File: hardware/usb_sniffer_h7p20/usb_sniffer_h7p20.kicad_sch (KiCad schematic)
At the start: 98 parts, among them J4 USB_C_Receptacle_USB2.0_16P, J5 FFC-40P-0.5mm,NC, U1 H7P20N0L128-M3H1, U6 P25Q32SH-SSH-IT, U7 CY7C68013A-56LTX, U8 24C64BN, U9 CJ3439KDW, X1 XO32,26M,NC, Y2 24M

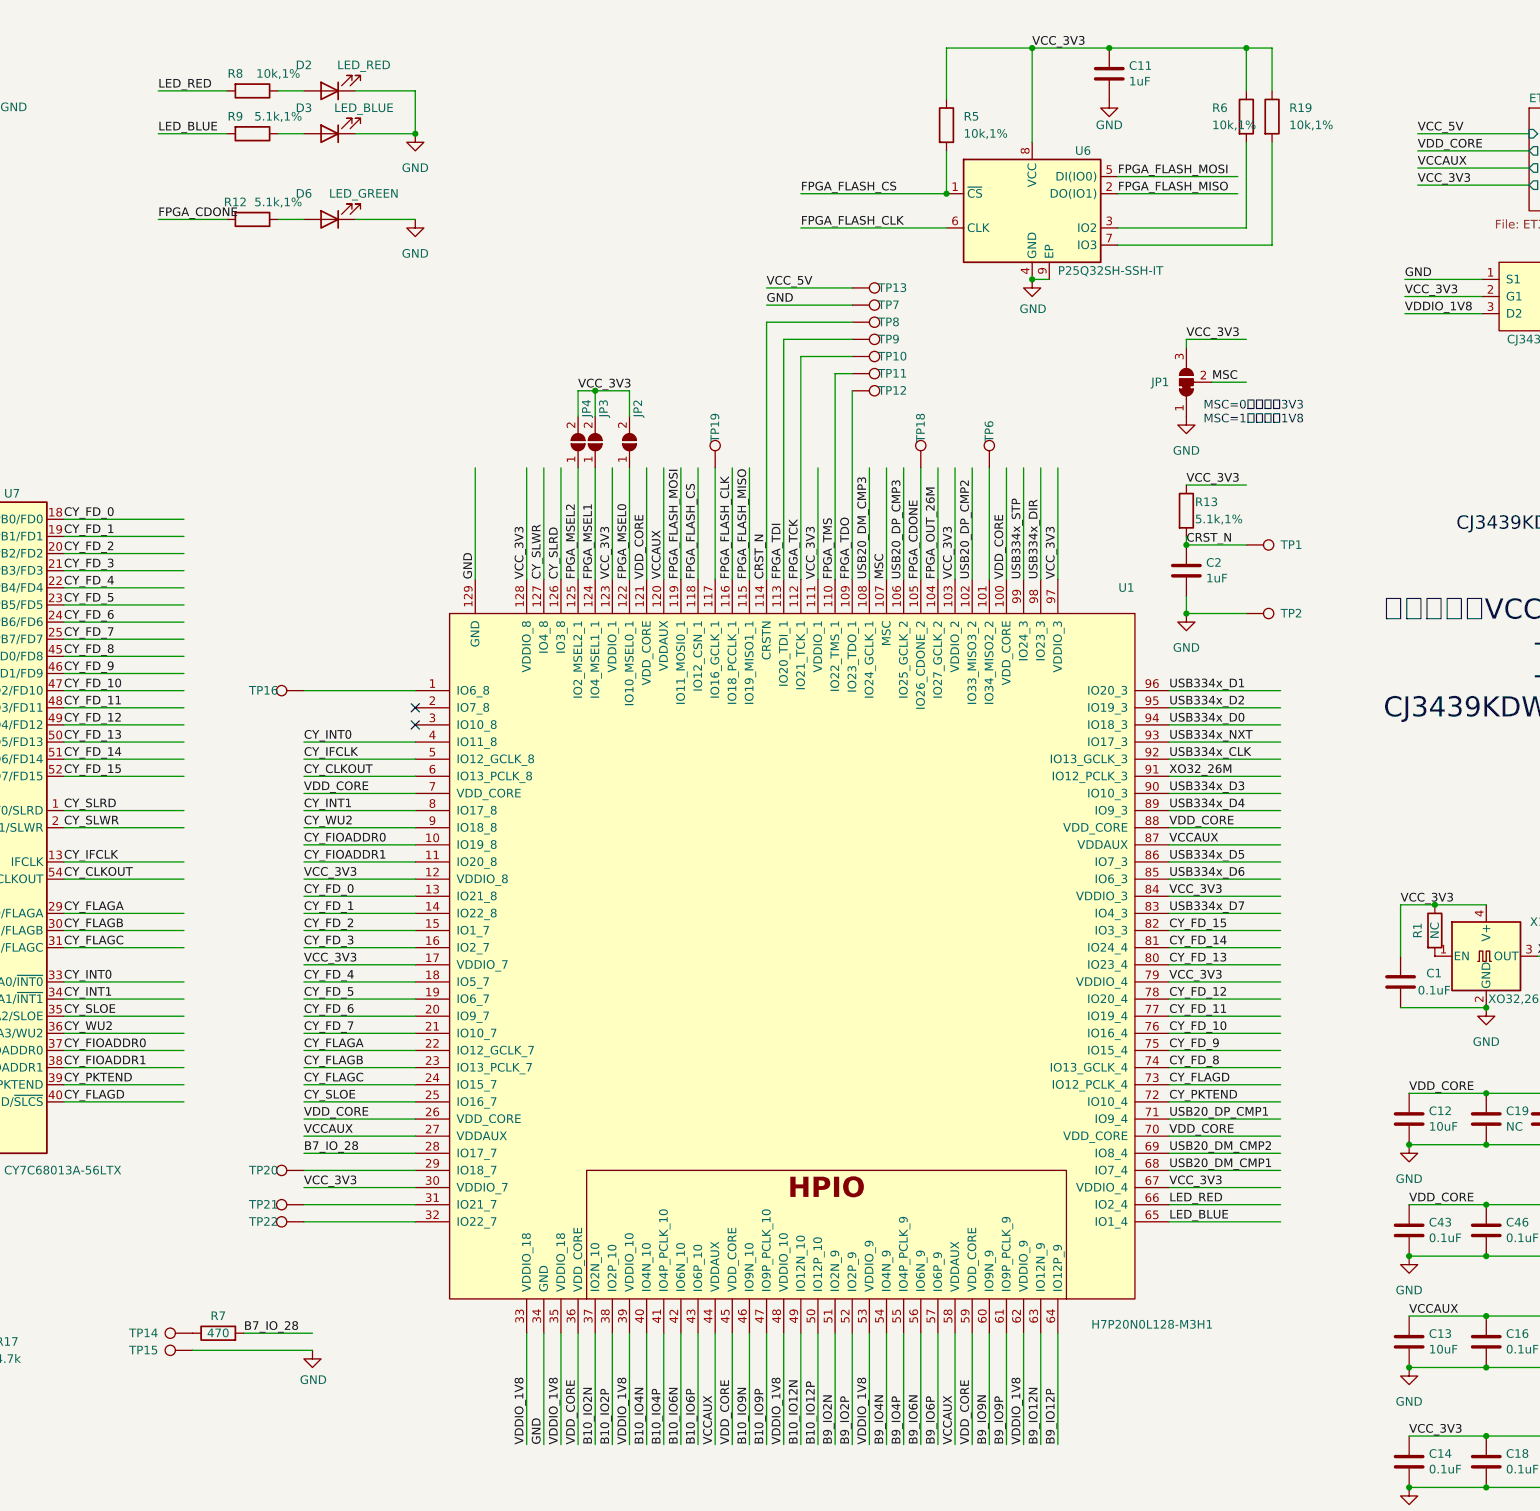
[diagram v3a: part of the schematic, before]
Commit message: [usb_sniffer_h7p20]增加JTAG排针，增加产品页二维码
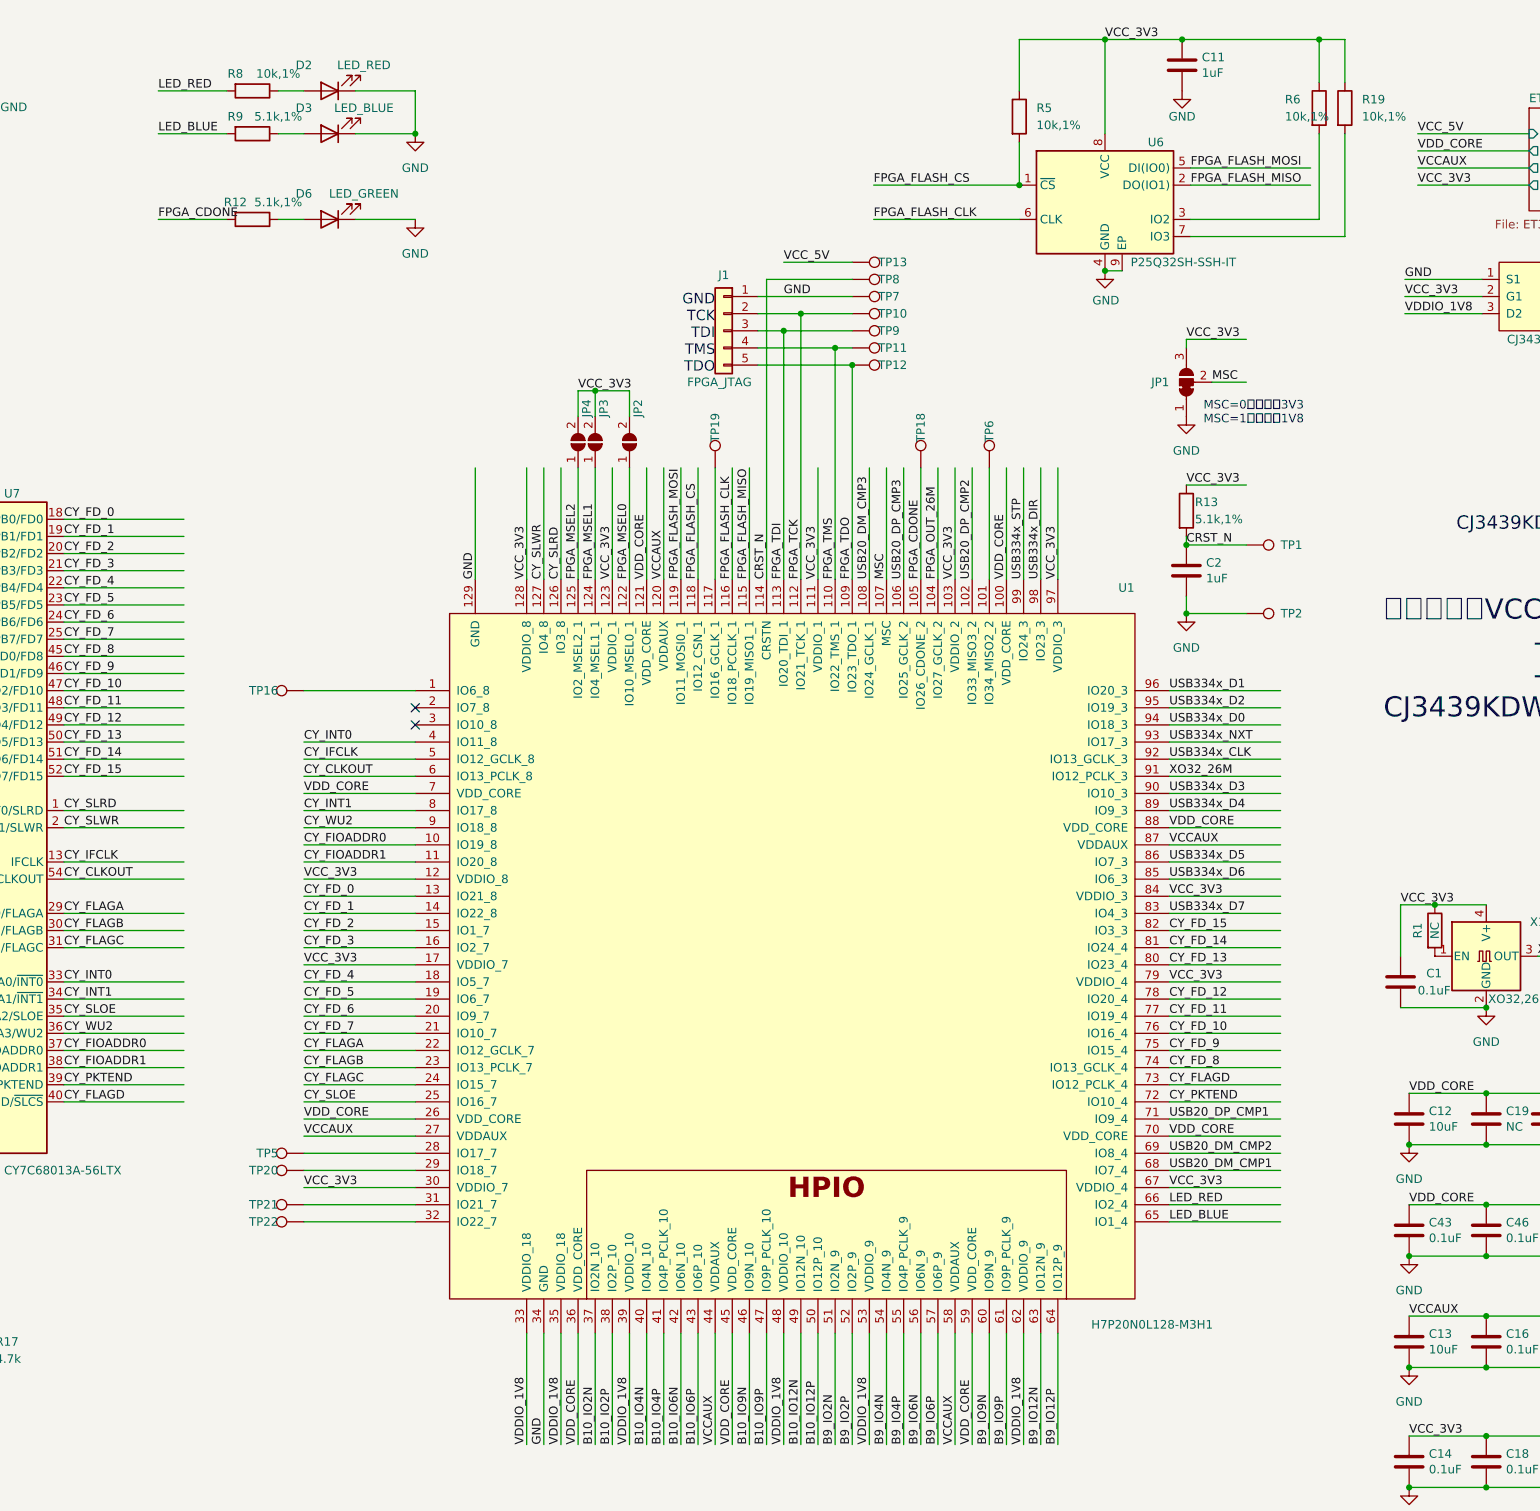
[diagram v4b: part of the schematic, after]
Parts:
- removed R7: 470, Resistor_SMD:R_0402_1005Metric, symbol Device:R
- removed TP14, TP15: TestPoint, vllogic:PinHeader_1x01_P1.00mm_Vertical, symbol Connector:TestPoint
- added J1: FPGA_JTAG, Connector_PinHeader_2.54mm:PinHeader_1x05_P2.54mm_Vertical, symbol Connector_Generic:Conn_01x05
- added TP5: TestPoint, vllogic:TestPoint_Pad_D0.3mm, symbol Connector:TestPoint
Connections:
- net FPGA_TCK: now also J1.2 (Pin_2)
- net FPGA_TDI: now also J1.3 (Pin_3)
- net FPGA_TDO: now also J1.5 (Pin_5)
- net FPGA_TMS: now also J1.4 (Pin_4)
- net GND: now also J1.1 (Pin_1)
- net B7_IO_28: no longer names the net of U1.28 (IO17_7)
- net B7_IO_28: now also TP5.1
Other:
- note added: "GND TCK TDI TMS TDO"
- moved on the sheet: C11, R19, R5, R6, TP10, TP11, TP12, TP13, TP7, TP8, TP9, U6
